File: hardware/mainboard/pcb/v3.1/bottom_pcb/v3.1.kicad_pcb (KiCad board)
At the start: 2 copper layers, 110 x 175 mm, 63 parts, among them J1 Conn_01x03_Male, J2 Conn_01x03_Male, U1 ATtiny1626, U10 TPIC6C595, U11 touch_but_square, U12 touch_but_square, U13 touch_but_square, U15 touch_but_square, U16 touch_but_square, U17 touch_but_square, U18 touch_but_square, U19 74hc4066, U2 ATtiny1626, U20 74hc4066, U21 74hc14d, U22 touch_but_square, U23 touch_but_square, U24 touch_but_square, U25 touch_but_square, U26 touch_but_square, U27 touch_but_square, U28 touch_but_square, U29 touch_but_square, U3 TPIC6C595, U30 74hc4066, U31 74hc4066, U32 touch_but_round, U33 touch_but_round, U34 touch_but_round, U4 TPIC6C595, U5 TPIC6C595, U6 TPIC6C595, U7 TPIC6C595, U8 TPIC6C595, U9 TPIC6C595

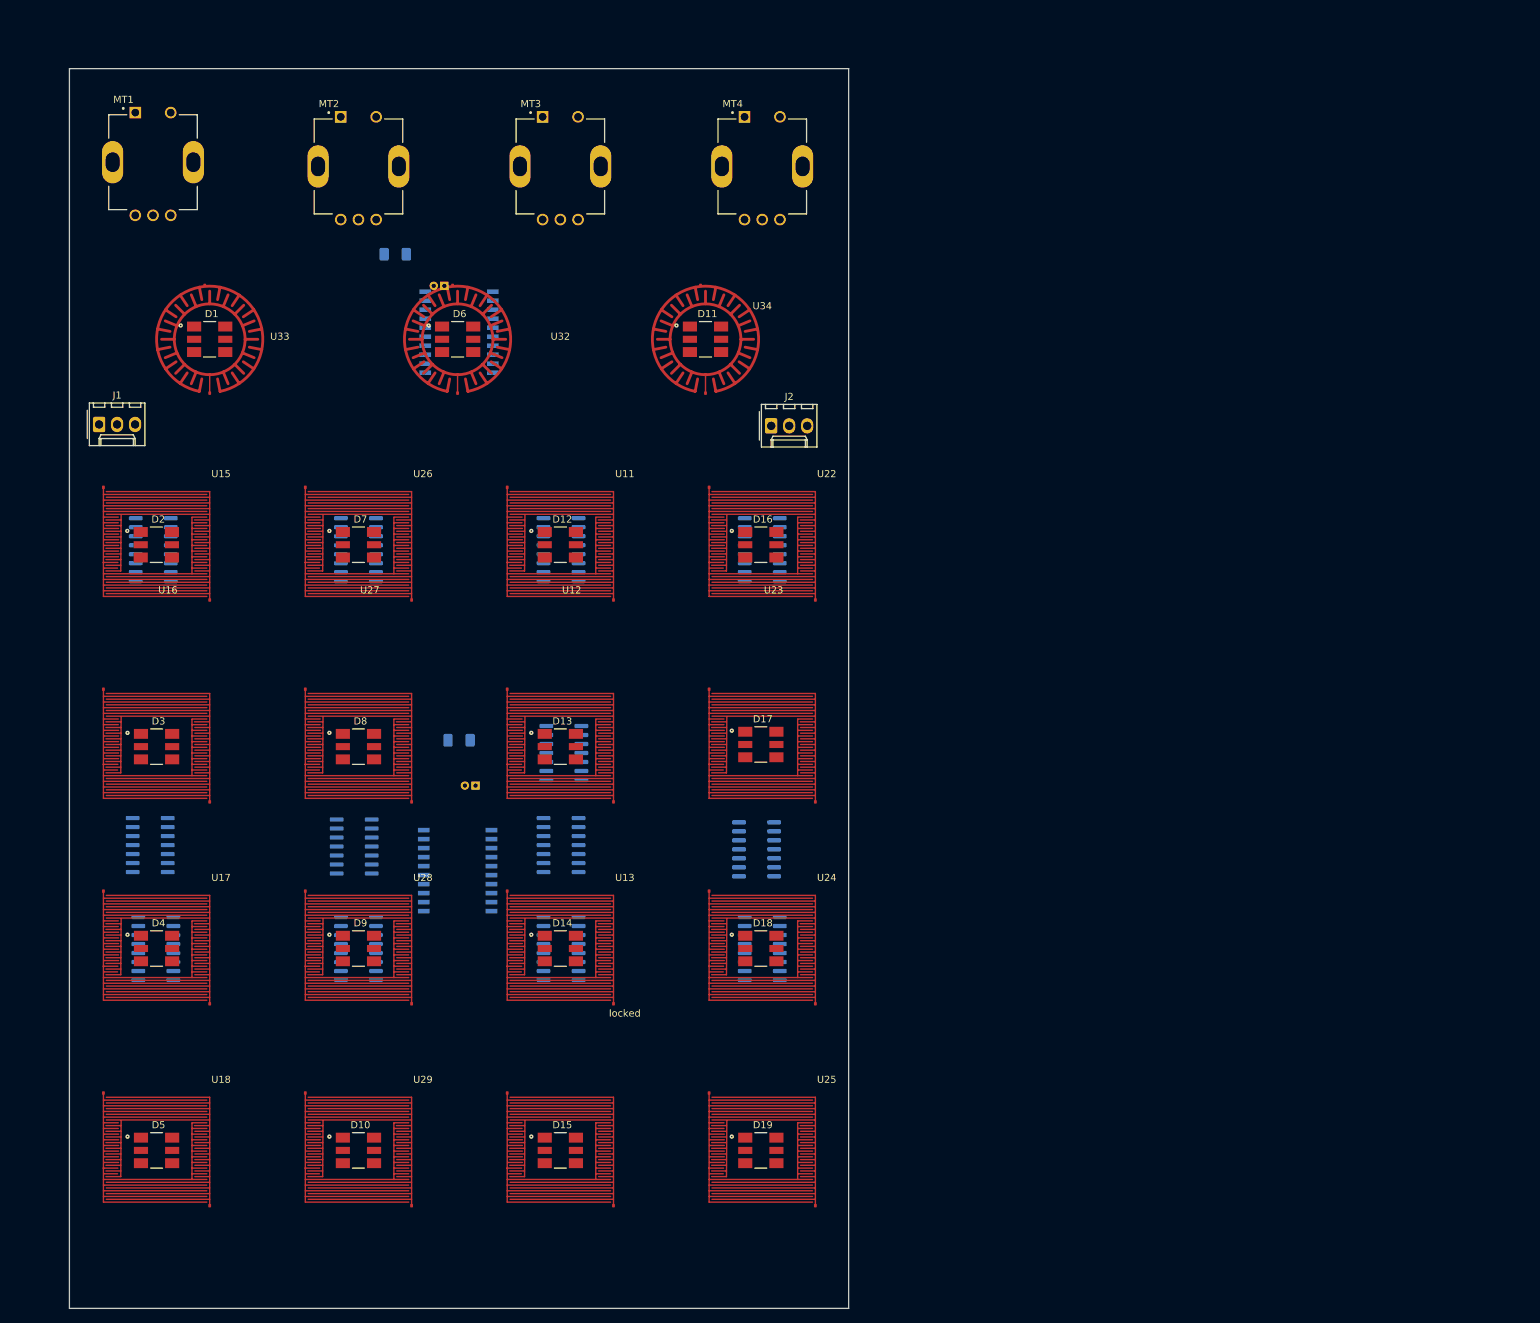
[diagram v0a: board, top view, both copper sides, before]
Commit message: pcb cut off
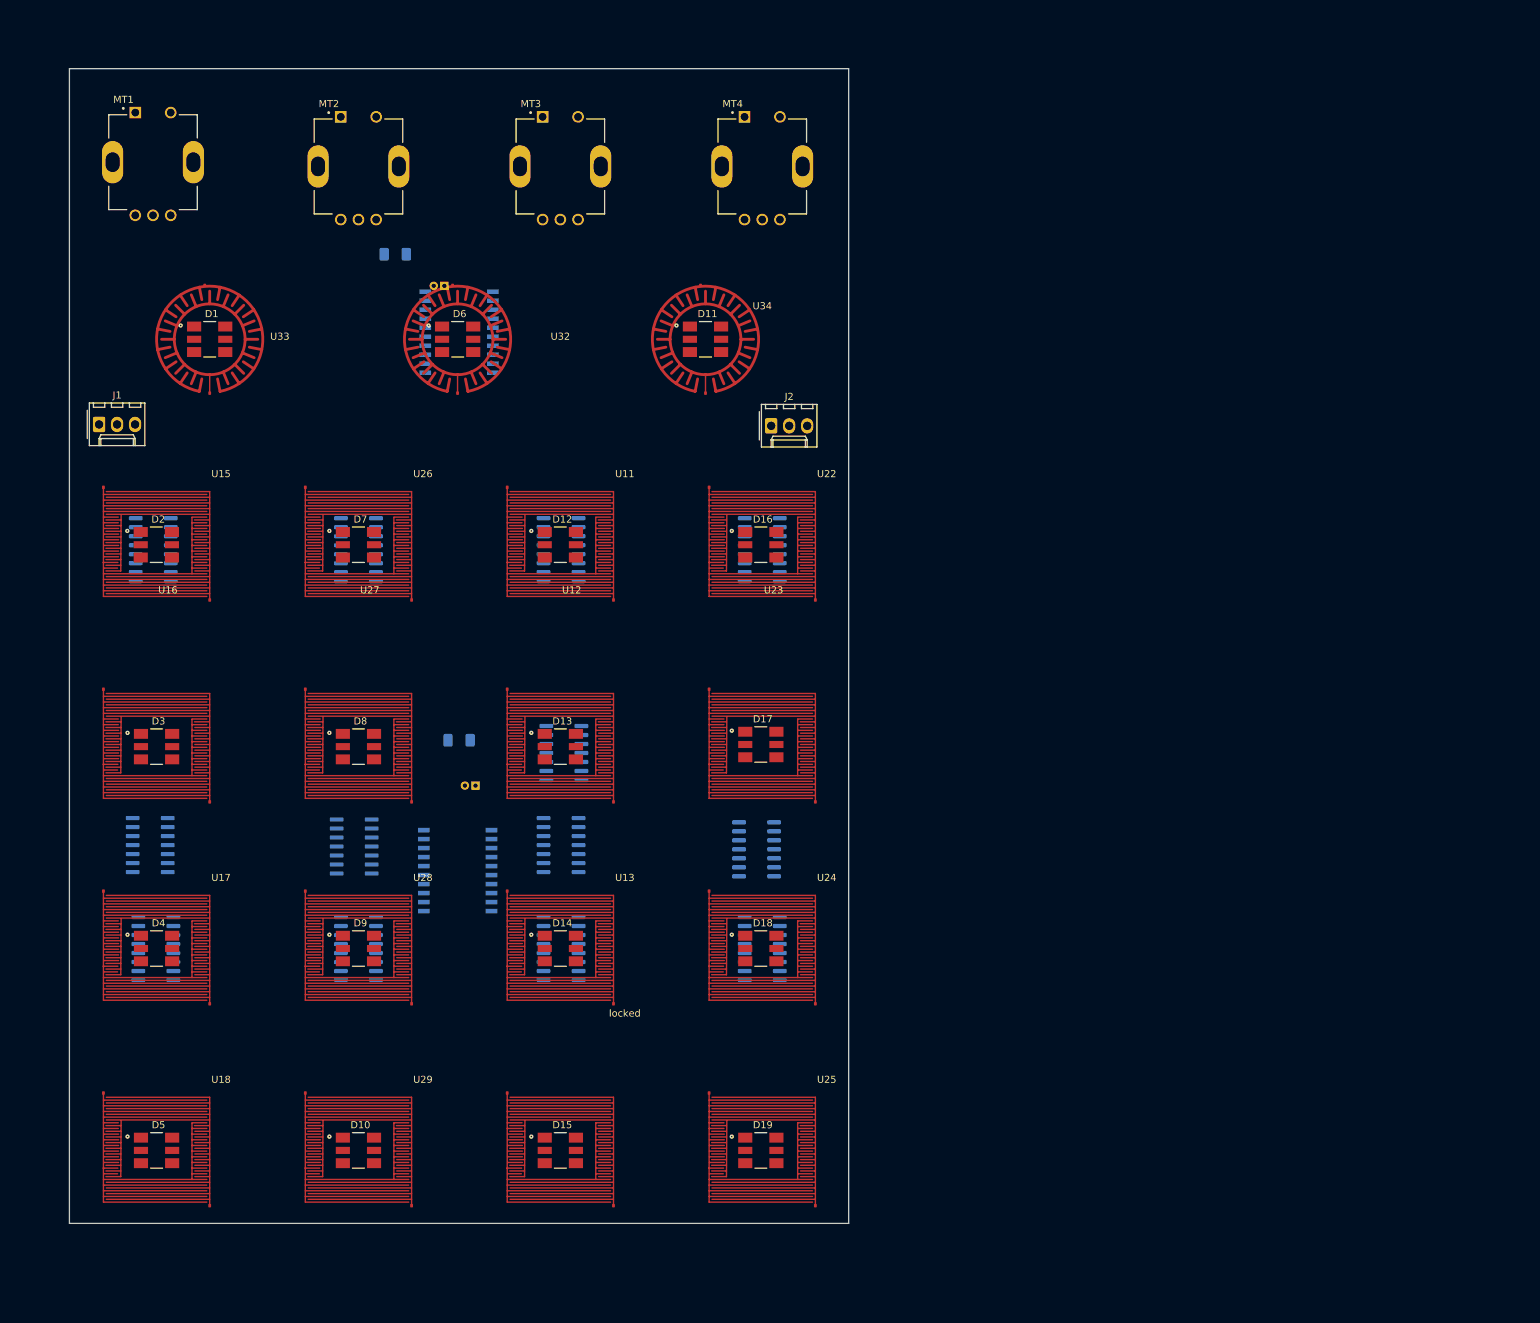
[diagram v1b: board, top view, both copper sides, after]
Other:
- board size 110 x 175 mm -> 110 x 163 mm
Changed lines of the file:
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@@
     )
   )
-  (gr_line locked (start 150 25) (end 150 200)
+  (gr_line locked (start 150 25) (end 150 188)
     (stroke (width 0.1) (type solid)) (layer "Edge.Cuts"))
-  (gr_line locked (start 40 200) (end 40 25)
+  (gr_line locked (start 40 188) (end 40 25)
     (stroke (width 0.1) (type solid)) (layer "Edge.Cuts"))
   (gr_line locked (start 40 25) (end 150 25)
     (stroke (width 0.1) (type solid)) (layer "Edge.Cuts"))
-  (gr_line locked (start 150 200) (end 40 200)
+  (gr_line locked (start 150 188) (end 40 188)
     (stroke (width 0.1) (type solid)) (layer "Edge.Cuts"))
 )

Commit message: .
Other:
- board size 110 x 163 mm -> 125.5 x 163 mm
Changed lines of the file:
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@@
     )
   )
-  (gr_line locked (start 150 25) (end 150 188)
+  (gr_line locked (start 157.75 25) (end 157.75 188)
     (stroke (width 0.1) (type solid)) (layer "Edge.Cuts"))
-  (gr_line locked (start 40 188) (end 40 25)
+  (gr_line locked (start 32.25 188) (end 32.25 25)
     (stroke (width 0.1) (type solid)) (layer "Edge.Cuts"))
-  (gr_line locked (start 40 25) (end 150 25)
+  (gr_line locked (start 32.25 25) (end 157.75 25)
     (stroke (width 0.1) (type solid)) (layer "Edge.Cuts"))
-  (gr_line locked (start 150 188) (end 40 188)
+  (gr_line locked (start 157.75 188) (end 32.25 188)
     (stroke (width 0.1) (type solid)) (layer "Edge.Cuts"))
 )

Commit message: update to 74hc4053aft
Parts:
- removed U30, U31: 74hc4066, Package_SO:SOIC-14_3.9x8.7mm_P1.27mm
- added C10: 100nF, Capacitor_SMD:C_1206_3216Metric_Pad1.33x1.80mm_HandSolder, F.Cu at (214.4, 36.9)
- added C11: 100nF, Capacitor_SMD:C_1206_3216Metric_Pad1.33x1.80mm_HandSolder, F.Cu at (214.4, 40.3)
- added C12: 100nF, Capacitor_SMD:C_1206_3216Metric_Pad1.33x1.80mm_HandSolder, F.Cu at (214.4, 43.6)
- added C13: 10nF, Capacitor_SMD:C_1206_3216Metric_Pad1.33x1.80mm_HandSolder, F.Cu at (222.4, 42.2)
- added C14: 10nF, Capacitor_SMD:C_1206_3216Metric_Pad1.33x1.80mm_HandSolder, F.Cu at (222.4, 45.5)
- added C15: 10nF, Capacitor_SMD:C_1206_3216Metric_Pad1.33x1.80mm_HandSolder, F.Cu at (222.4, 48.9)
- added C16: 10nF, Capacitor_SMD:C_1206_3216Metric_Pad1.33x1.80mm_HandSolder, F.Cu at (222.4, 52.2)
- added C17: 10nF, Capacitor_SMD:C_1206_3216Metric_Pad1.33x1.80mm_HandSolder, F.Cu at (222.4, 55.6)
- added C18: 10nF, Capacitor_SMD:C_1206_3216Metric_Pad1.33x1.80mm_HandSolder, F.Cu at (222.4, 58.9)
- added C19: 10nF, Capacitor_SMD:C_1206_3216Metric_Pad1.33x1.80mm_HandSolder, F.Cu at (222.4, 62.3)
- added C21: 10nF, Capacitor_SMD:C_1206_3216Metric_Pad1.33x1.80mm_HandSolder, F.Cu at (222.4, 65.6)
- added C5: 100nF, Capacitor_SMD:C_1206_3216Metric_Pad1.33x1.80mm_HandSolder, F.Cu at (214.4, 20.2)
- added C6: 100nF, Capacitor_SMD:C_1206_3216Metric_Pad1.33x1.80mm_HandSolder, F.Cu at (214.4, 23.5)
- added C7: 100nF, Capacitor_SMD:C_1206_3216Metric_Pad1.33x1.80mm_HandSolder, F.Cu at (214.4, 26.9)
- added C8: 100nF, Capacitor_SMD:C_1206_3216Metric_Pad1.33x1.80mm_HandSolder, F.Cu at (214.4, 30.2)
- added C9: 100nF, Capacitor_SMD:C_1206_3216Metric_Pad1.33x1.80mm_HandSolder, F.Cu at (214.4, 33.6)
- added R1: R, Resistor_SMD:R_1206_3216Metric, F.Cu at (180.5, 20.2)
- added R10: R, Resistor_SMD:R_1206_3216Metric, F.Cu at (180.5, 49.8)
- added R100: 10k, Resistor_SMD:R_1206_3216Metric_Pad1.30x1.75mm_HandSolder, F.Cu at (234.3, 45.4)
- added R101: 10k, Resistor_SMD:R_1206_3216Metric_Pad1.30x1.75mm_HandSolder, F.Cu at (234.3, 48.7)
- added R102: 10k, Resistor_SMD:R_1206_3216Metric_Pad1.30x1.75mm_HandSolder, F.Cu at (234.3, 52.0)
- added R103: 10k, Resistor_SMD:R_1206_3216Metric_Pad1.30x1.75mm_HandSolder, F.Cu at (234.3, 55.3)
- added R104: 10k, Resistor_SMD:R_1206_3216Metric_Pad1.30x1.75mm_HandSolder, F.Cu at (234.3, 58.6)
- added R105: 10k, Resistor_SMD:R_1206_3216Metric_Pad1.30x1.75mm_HandSolder, F.Cu at (234.3, 61.9)
- added R106: 10k, Resistor_SMD:R_1206_3216Metric_Pad1.30x1.75mm_HandSolder, F.Cu at (240.2, 42.1)
- added R107: 10k, Resistor_SMD:R_1206_3216Metric_Pad1.30x1.75mm_HandSolder, F.Cu at (240.2, 45.4)
- added R108: 10k, Resistor_SMD:R_1206_3216Metric_Pad1.30x1.75mm_HandSolder, F.Cu at (240.2, 48.7)
- added R109: 10k, Resistor_SMD:R_1206_3216Metric_Pad1.30x1.75mm_HandSolder, F.Cu at (240.2, 52.0)
- added R11: R, Resistor_SMD:R_1206_3216Metric, F.Cu at (186.1, 20.2)
- added R110: 10k, Resistor_SMD:R_1206_3216Metric_Pad1.30x1.75mm_HandSolder, F.Cu at (240.2, 55.3)
- added R111: 10k, Resistor_SMD:R_1206_3216Metric_Pad1.30x1.75mm_HandSolder, F.Cu at (240.2, 58.6)
- added R12: R, Resistor_SMD:R_1206_3216Metric, F.Cu at (186.1, 23.4)
- added R13: R, Resistor_SMD:R_1206_3216Metric, F.Cu at (186.1, 26.7)
- added R14: R, Resistor_SMD:R_1206_3216Metric, F.Cu at (186.1, 30.0)
- added R15: R, Resistor_SMD:R_1206_3216Metric, F.Cu at (186.1, 33.3)
- added R16: R, Resistor_SMD:R_1206_3216Metric, F.Cu at (186.1, 36.6)
- added R17: R, Resistor_SMD:R_1206_3216Metric, F.Cu at (186.1, 39.9)
- added R18: R, Resistor_SMD:R_1206_3216Metric, F.Cu at (186.1, 43.2)
- added R19: R, Resistor_SMD:R_1206_3216Metric, F.Cu at (186.1, 46.5)
- added R2: R, Resistor_SMD:R_1206_3216Metric, F.Cu at (180.5, 23.4)
- added R20: R, Resistor_SMD:R_1206_3216Metric, F.Cu at (186.1, 49.8)
- added R21: R, Resistor_SMD:R_1206_3216Metric, F.Cu at (191.7, 20.2)
- added R22: R, Resistor_SMD:R_1206_3216Metric, F.Cu at (191.7, 23.4)
- added R23: R, Resistor_SMD:R_1206_3216Metric, F.Cu at (191.7, 26.7)
- added R24: R, Resistor_SMD:R_1206_3216Metric, F.Cu at (191.7, 30.0)
- added R25: R, Resistor_SMD:R_1206_3216Metric, F.Cu at (191.7, 33.3)
- added R26: R, Resistor_SMD:R_1206_3216Metric, F.Cu at (191.7, 36.6)
- added R27: R, Resistor_SMD:R_1206_3216Metric, F.Cu at (191.7, 39.9)
- added R28: R, Resistor_SMD:R_1206_3216Metric, F.Cu at (191.7, 43.2)
- added R29: R, Resistor_SMD:R_1206_3216Metric, F.Cu at (191.7, 46.5)
- added R3: R, Resistor_SMD:R_1206_3216Metric, F.Cu at (180.5, 26.7)
- added R30: R, Resistor_SMD:R_1206_3216Metric, F.Cu at (191.7, 49.8)
- added R31: 0R, Resistor_SMD:R_1206_3216Metric_Pad1.30x1.75mm_HandSolder, F.Cu at (180.7, 53.1)
- added R32: 0R, Resistor_SMD:R_1206_3216Metric_Pad1.30x1.75mm_HandSolder, F.Cu at (180.7, 56.4)
- added R33: 4K7, Resistor_SMD:R_1206_3216Metric_Pad1.30x1.75mm_HandSolder, F.Cu at (180.7, 59.6)
- added R34: 4K7, Resistor_SMD:R_1206_3216Metric_Pad1.30x1.75mm_HandSolder, F.Cu at (180.7, 62.9)
- added R35: 0R, Resistor_SMD:R_1206_3216Metric_Pad1.30x1.75mm_HandSolder, F.Cu at (180.7, 66.2)
- added R36: 0R, Resistor_SMD:R_1206_3216Metric_Pad1.30x1.75mm_HandSolder, F.Cu at (186.6, 53.1)
- added R37: R, Resistor_SMD:R_1206_3216Metric, F.Cu at (197.3, 20.2)
- added R38: R, Resistor_SMD:R_1206_3216Metric, F.Cu at (197.3, 23.4)
- added R39: R, Resistor_SMD:R_1206_3216Metric, F.Cu at (197.3, 26.7)
- added R4: R, Resistor_SMD:R_1206_3216Metric, F.Cu at (180.5, 30.0)
- added R40: R, Resistor_SMD:R_1206_3216Metric, F.Cu at (197.3, 30.0)
- added R41: R, Resistor_SMD:R_1206_3216Metric, F.Cu at (197.3, 33.3)
- added R42: R, Resistor_SMD:R_1206_3216Metric, F.Cu at (197.3, 36.6)
- added R43: R, Resistor_SMD:R_1206_3216Metric, F.Cu at (197.3, 39.9)
- added R44: R, Resistor_SMD:R_1206_3216Metric, F.Cu at (197.3, 43.2)
- added R45: R, Resistor_SMD:R_1206_3216Metric, F.Cu at (197.3, 46.5)
- added R46: R, Resistor_SMD:R_1206_3216Metric, F.Cu at (197.3, 49.8)
- added R47: R, Resistor_SMD:R_1206_3216Metric, F.Cu at (202.9, 20.2)
- added R48: R, Resistor_SMD:R_1206_3216Metric, F.Cu at (202.9, 23.4)
- added R49: R, Resistor_SMD:R_1206_3216Metric, F.Cu at (202.9, 26.7)
- added R5: R, Resistor_SMD:R_1206_3216Metric, F.Cu at (180.5, 33.3)
- added R50: R, Resistor_SMD:R_1206_3216Metric, F.Cu at (202.9, 30.0)
- added R51: R, Resistor_SMD:R_1206_3216Metric, F.Cu at (202.9, 33.3)
- added R52: 4K7, Resistor_SMD:R_1206_3216Metric_Pad1.30x1.75mm_HandSolder, F.Cu at (186.6, 56.4)
- added R53: 4K7, Resistor_SMD:R_1206_3216Metric_Pad1.30x1.75mm_HandSolder, F.Cu at (186.6, 59.6)
- added R54: 0R, Resistor_SMD:R_1206_3216Metric_Pad1.30x1.75mm_HandSolder, F.Cu at (186.6, 62.9)
- added R55: 0R, Resistor_SMD:R_1206_3216Metric_Pad1.30x1.75mm_HandSolder, F.Cu at (186.6, 66.2)
- added R56: 4K7, Resistor_SMD:R_1206_3216Metric_Pad1.30x1.75mm_HandSolder, F.Cu at (192.6, 53.1)
- added R57: 4K7, Resistor_SMD:R_1206_3216Metric_Pad1.30x1.75mm_HandSolder, F.Cu at (192.6, 56.4)
- added R58: R, Resistor_SMD:R_1206_3216Metric, F.Cu at (202.9, 36.6)
- added R59: R, Resistor_SMD:R_1206_3216Metric, F.Cu at (202.9, 39.9)
- added R6: R, Resistor_SMD:R_1206_3216Metric, F.Cu at (180.5, 36.6)
- added R60: R, Resistor_SMD:R_1206_3216Metric, F.Cu at (202.9, 43.2)
- added R61: R, Resistor_SMD:R_1206_3216Metric, F.Cu at (202.9, 46.5)
- added R62: R, Resistor_SMD:R_1206_3216Metric, F.Cu at (202.9, 49.8)
- added R63: R, Resistor_SMD:R_1206_3216Metric, F.Cu at (208.6, 20.2)
- added R64: R, Resistor_SMD:R_1206_3216Metric, F.Cu at (208.6, 23.4)
- added R65: R, Resistor_SMD:R_1206_3216Metric, F.Cu at (208.6, 26.7)
- added R66: R, Resistor_SMD:R_1206_3216Metric, F.Cu at (208.6, 30.0)
- added R67: R, Resistor_SMD:R_1206_3216Metric, F.Cu at (208.6, 33.3)
- added R68: R, Resistor_SMD:R_1206_3216Metric, F.Cu at (208.6, 36.6)
- added R69: R, Resistor_SMD:R_1206_3216Metric, F.Cu at (208.6, 39.9)
- added R7: R, Resistor_SMD:R_1206_3216Metric, F.Cu at (180.5, 39.9)
- added R70: 0R, Resistor_SMD:R_1206_3216Metric_Pad1.30x1.75mm_HandSolder, F.Cu at (192.6, 59.6)
- added R71: 4K7, Resistor_SMD:R_1206_3216Metric_Pad1.30x1.75mm_HandSolder, F.Cu at (192.6, 62.9)
- added R72: 4K7, Resistor_SMD:R_1206_3216Metric_Pad1.30x1.75mm_HandSolder, F.Cu at (192.6, 66.2)
- added R73: R, Resistor_SMD:R_1206_3216Metric_Pad1.30x1.75mm_HandSolder, F.Cu at (231.5, 20.2)
- added R74: R, Resistor_SMD:R_1206_3216Metric_Pad1.30x1.75mm_HandSolder, F.Cu at (231.5, 23.4)
- added R75: R, Resistor_SMD:R_1206_3216Metric_Pad1.30x1.75mm_HandSolder, F.Cu at (231.5, 26.7)
- added R76: R, Resistor_SMD:R_1206_3216Metric_Pad1.30x1.75mm_HandSolder, F.Cu at (231.5, 30.0)
- added R77: R, Resistor_SMD:R_1206_3216Metric_Pad1.30x1.75mm_HandSolder, F.Cu at (231.5, 33.3)
- added R78: R, Resistor_SMD:R_1206_3216Metric_Pad1.30x1.75mm_HandSolder, F.Cu at (231.5, 36.6)
- added R79: R, Resistor_SMD:R_1206_3216Metric_Pad1.30x1.75mm_HandSolder, F.Cu at (237.4, 20.2)
- added R8: R, Resistor_SMD:R_1206_3216Metric, F.Cu at (180.5, 43.2)
- added R80: R, Resistor_SMD:R_1206_3216Metric_Pad1.30x1.75mm_HandSolder, F.Cu at (237.4, 23.4)
- added R81: R, Resistor_SMD:R_1206_3216Metric_Pad1.30x1.75mm_HandSolder, F.Cu at (237.4, 26.7)
- added R82: R, Resistor_SMD:R_1206_3216Metric_Pad1.30x1.75mm_HandSolder, F.Cu at (237.4, 30.0)
- added R83: R, Resistor_SMD:R_1206_3216Metric_Pad1.30x1.75mm_HandSolder, F.Cu at (237.4, 33.3)
- added R84: R, Resistor_SMD:R_1206_3216Metric_Pad1.30x1.75mm_HandSolder, F.Cu at (237.4, 36.6)
- added R85: R, Resistor_SMD:R_1206_3216Metric_Pad1.30x1.75mm_HandSolder, F.Cu at (243.4, 20.2)
- added R86: R, Resistor_SMD:R_1206_3216Metric_Pad1.30x1.75mm_HandSolder, F.Cu at (243.4, 23.4)
- added R87: R, Resistor_SMD:R_1206_3216Metric_Pad1.30x1.75mm_HandSolder, F.Cu at (243.4, 26.7)
- added R88: R, Resistor_SMD:R_1206_3216Metric_Pad1.30x1.75mm_HandSolder, F.Cu at (243.4, 30.0)
- added R89: 10k, Resistor_SMD:R_1206_3216Metric_Pad1.30x1.75mm_HandSolder, F.Cu at (228.3, 42.1)
- added R9: R, Resistor_SMD:R_1206_3216Metric, F.Cu at (180.5, 46.5)
- added R90: 10k, Resistor_SMD:R_1206_3216Metric_Pad1.30x1.75mm_HandSolder, F.Cu at (228.3, 45.4)
- added R91: 10k, Resistor_SMD:R_1206_3216Metric_Pad1.30x1.75mm_HandSolder, F.Cu at (228.3, 48.7)
- added R92: 10k, Resistor_SMD:R_1206_3216Metric_Pad1.30x1.75mm_HandSolder, F.Cu at (228.3, 52.0)
- added R93: 10k, Resistor_SMD:R_1206_3216Metric_Pad1.30x1.75mm_HandSolder, F.Cu at (228.3, 55.3)
- added R94: 10k, Resistor_SMD:R_1206_3216Metric_Pad1.30x1.75mm_HandSolder, F.Cu at (228.3, 58.6)
- added R95: R, Resistor_SMD:R_1206_3216Metric_Pad1.30x1.75mm_HandSolder, F.Cu at (222.3, 71.0)
- added R96: R, Resistor_SMD:R_1206_3216Metric_Pad1.30x1.75mm_HandSolder, F.Cu at (222.3, 74.2)
- added R97: R, Resistor_SMD:R_1206_3216Metric_Pad1.30x1.75mm_HandSolder, F.Cu at (222.3, 77.5)
- added R98: 10k, Resistor_SMD:R_1206_3216Metric_Pad1.30x1.75mm_HandSolder, F.Cu at (228.3, 61.9)
- added R99: 10k, Resistor_SMD:R_1206_3216Metric_Pad1.30x1.75mm_HandSolder, F.Cu at (234.3, 42.1)
- U19, U20: value 74hc4066 -> 74VHC4053AFT; footprint Package_SO:SOIC-14_3.9x8.7mm_P1.27mm -> 3dAudioFoot:74vhc4053aft; moved to F.Cu
- U21: value 74hc14d -> 74VHC4053AFT; footprint Package_SO:SOIC-14_3.9x8.7mm_P1.27mm -> 3dAudioFoot:74vhc4053aft; moved to F.Cu
- moved U20 82.1 mm to (128.6, 106.8), turned to 0 degrees
- moved U19 48.5 mm to (68.4, 108.6), turned to 0 degrees
- moved U21 38.6 mm to (95.8, 157.6), turned to 0 degrees
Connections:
- MT1 pad A: EA1 -> Net-(MT1-PadA)
- MT1 pad B: EB1 -> Net-(MT1-PadB)
- MT2 pad A: EA2 -> Net-(MT2-PadA)
- MT2 pad B: EB2 -> Net-(MT2-PadB)
- MT3 pad A: /Encoder/ENCA3 -> Net-(MT3-PadA)
- MT3 pad B: /Encoder/ENCB3 -> Net-(MT3-PadB)
- MT4 pad A: /Encoder/ENCA4 -> Net-(MT4-PadA)
- MT4 pad B: /Encoder/ENCB4 -> Net-(MT4-PadB)
- U11 pad 1: Net-(R77-Pad2) -> BUTB1
- U12 pad 1: Net-(R78-Pad2) -> BUTB2
- U13 pad 1: Net-(R79-Pad2) -> BUTB3
- U15 pad 1: Net-(R73-Pad2) -> BUTA1
- U16 pad 1: Net-(R74-Pad2) -> BUTA2
- U17 pad 1: Net-(R75-Pad2) -> BUTA3
- U18 pad 1: Net-(R76-Pad2) -> BUTA4
- U19 pad 1: Net-(R77-Pad2) -> BUTB2
- U19 pad 10: /Button round/BUTCD4 -> /Button round/BUTAB2
- U19 pad 11: Net-(R80-Pad2) -> /Button round/BUTAB1
- U19 pad 12: /Button round/BUT_CTL -> BUTA1
- U19 pad 13: /Button round/BUT_CTL -> BUTB1
- U19 pad 14: +5V -> /Button round/BUT_CTL
- U19 pad 2: /Button round/BUTCD1 -> BUTA2
- U19 pad 3: /Button round/BUTCD2 -> BUTB3
- U19 pad 4: Net-(R78-Pad2) -> /Button round/BUT_CTL
- U19 pad 5: /Button round/BUT_CTL -> BUTA3
- U19 pad 6: /Button round/BUT_CTL -> GND
- U19 pad 8: Net-(R79-Pad2) -> GND
- U19 pad 9: /Button round/BUTCD3 -> /Button round/BUTAB3
- U20 pad 1: Net-(R73-Pad2) -> BUTD2
- U20 pad 10: /Button round/BUTAB4 -> /Button round/BUTCD2
- U20 pad 11: Net-(R76-Pad2) -> /Button round/BUTCD1
- U20 pad 12: /Button round/BUT_CTL -> BUTC1
- U20 pad 13: /Button round/BUT_CTL -> BUTD1
- U20 pad 14: +5V -> /Button round/BUT_CTL
- U20 pad 2: /Button round/BUTAB1 -> BUTC2
- U20 pad 3: /Button round/BUTAB2 -> BUTD3
- U20 pad 4: Net-(R74-Pad2) -> /Button round/BUT_CTL
- U20 pad 5: /Button round/BUT_CTL -> BUTC3
- U20 pad 6: /Button round/BUT_CTL -> GND
- U20 pad 8: Net-(R75-Pad2) -> GND
- U20 pad 9: /Button round/BUTAB3 -> /Button round/BUTCD3
- U21 pad 1: /Button round/BUT_CTL -> unconnected-(U21-1Y-Pad1)
- U21 pad 11: unconnected-(U21-Pad11) -> /Button round/BUTCD4
- U21 pad 12: unconnected-(U21-Pad12) -> BUTC4
- U21 pad 13: unconnected-(U21-Pad13) -> BUTD4
- U21 pad 14: +5V -> /Button round/BUT_CTL
- U21 pad 2: BUT_CTL_I -> unconnected-(U21-0Y-Pad2)
- U21 pad 3: unconnected-(U21-Pad3) -> BUTB4
- U21 pad 4: unconnected-(U21-Pad4) -> /Button round/BUT_CTL
- U21 pad 5: unconnected-(U21-Pad5) -> BUTA4
- U21 pad 6: unconnected-(U21-Pad6) -> GND
- U21 pad 8: unconnected-(U21-Pad8) -> GND
- U21 pad 9: unconnected-(U21-Pad9) -> /Button round/BUTAB4
- U22 pad 1: Net-(R85-Pad2) -> BUTD1
- U23 pad 1: Net-(R86-Pad2) -> BUTD2
- U24 pad 1: Net-(R87-Pad2) -> BUTD3
- U25 pad 1: Net-(R88-Pad2) -> BUTD4
- U26 pad 1: Net-(R81-Pad2) -> BUTC1
- U27 pad 1: Net-(R82-Pad2) -> BUTC2
- U28 pad 1: Net-(R83-Pad2) -> BUTC3
- U29 pad 1: Net-(R84-Pad2) -> BUTC4
- locked pad 1: Net-(R80-Pad2) -> BUTB4
